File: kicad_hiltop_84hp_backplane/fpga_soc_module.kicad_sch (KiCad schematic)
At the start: 31 parts, among them J11 SO-DIMM

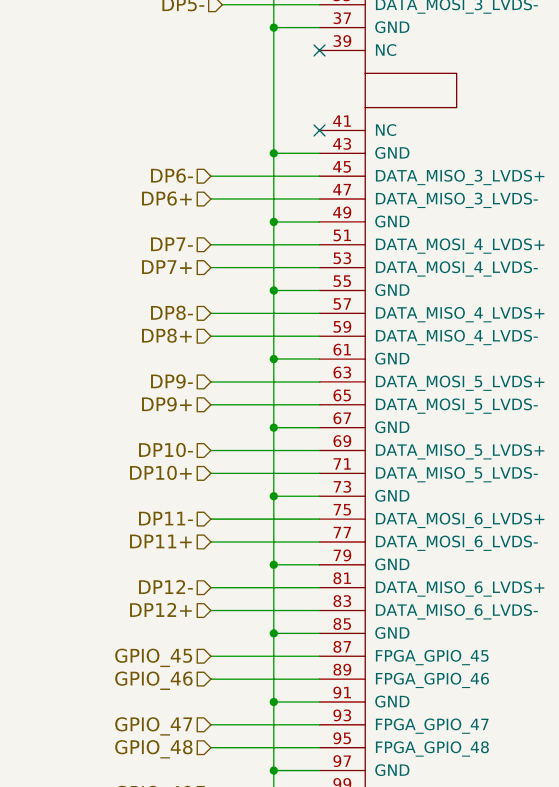
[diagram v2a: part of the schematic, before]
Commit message: Started differential tracking on layout
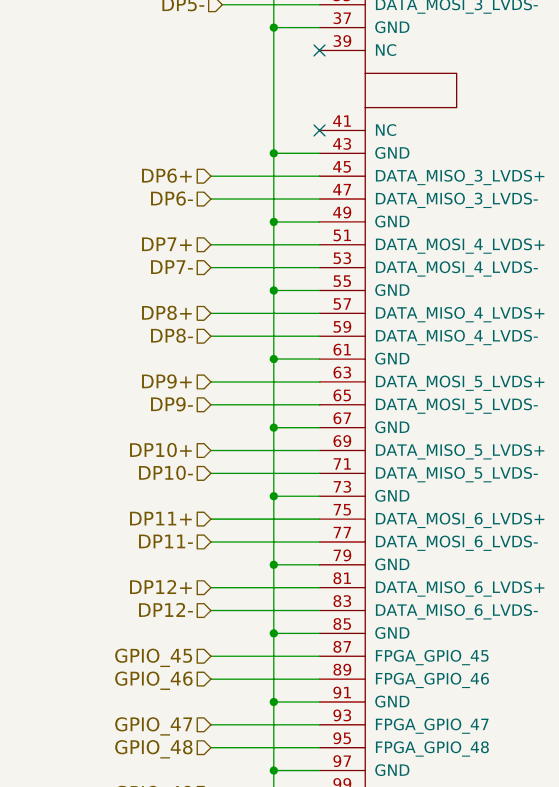
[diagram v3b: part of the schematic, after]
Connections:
- net DP10+: now also J11.69 (DATA_MISO_5_LVDS+); no longer J11.71 (DATA_MISO_5_LVDS-)
- net DP10-: now also J11.71 (DATA_MISO_5_LVDS-); no longer J11.69 (DATA_MISO_5_LVDS+)
- net DP11+: now also J11.75 (DATA_MOSI_6_LVDS+); no longer J11.77 (DATA_MOSI_6_LVDS-)
- net DP11-: now also J11.77 (DATA_MOSI_6_LVDS-); no longer J11.75 (DATA_MOSI_6_LVDS+)
- net DP12+: now also J11.81 (DATA_MISO_6_LVDS+); no longer J11.83 (DATA_MISO_6_LVDS-)
- net DP12-: now also J11.83 (DATA_MISO_6_LVDS-); no longer J11.81 (DATA_MISO_6_LVDS+)
- net DP6+: now also J11.45 (DATA_MISO_3_LVDS+); no longer J11.47 (DATA_MISO_3_LVDS-)
- net DP6-: now also J11.47 (DATA_MISO_3_LVDS-); no longer J11.45 (DATA_MISO_3_LVDS+)
- net DP7+: now also J11.51 (DATA_MOSI_4_LVDS+); no longer J11.53 (DATA_MOSI_4_LVDS-)
- net DP7-: now also J11.53 (DATA_MOSI_4_LVDS-); no longer J11.51 (DATA_MOSI_4_LVDS+)
- net DP8+: now also J11.57 (DATA_MISO_4_LVDS+); no longer J11.59 (DATA_MISO_4_LVDS-)
- net DP8-: now also J11.59 (DATA_MISO_4_LVDS-); no longer J11.57 (DATA_MISO_4_LVDS+)
- net DP9+: now also J11.63 (DATA_MOSI_5_LVDS+); no longer J11.65 (DATA_MOSI_5_LVDS-)
- net DP9-: now also J11.65 (DATA_MOSI_5_LVDS-); no longer J11.63 (DATA_MOSI_5_LVDS+)
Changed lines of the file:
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@@
     (effects (font (size 1.524 1.524)) (justify left))
   )
-  (hierarchical_label "DP6-" (shape input) (at 69.85 104.14 180)
+  (hierarchical_label "DP6-" (shape input) (at 69.85 106.68 180)
     (effects (font (size 1.524 1.524)) (justify right))
   )
@@
     (effects (font (size 1.524 1.524)) (justify left))
   )
-  (hierarchical_label "DP12-" (shape input) (at 69.85 149.86 180)
+  (hierarchical_label "DP12-" (shape input) (at 69.85 152.4 180)
     (effects (font (size 1.524 1.524)) (justify right))
   )
@@
     (effects (font (size 1.524 1.524)) (justify left))
   )
-  (hierarchical_label "DP10-" (shape input) (at 69.85 134.62 180)
+  (hierarchical_label "DP10-" (shape input) (at 69.85 137.16 180)
     (effects (font (size 1.524 1.524)) (justify right))
   )
@@
     (effects (font (size 1.524 1.524)) (justify left))
   )
-  (hierarchical_label "DP8-" (shape input) (at 69.85 119.38 180)
+  (hierarchical_label "DP8-" (shape input) (at 69.85 121.92 180)
     (effects (font (size 1.524 1.524)) (justify right))
   )
@@
     (effects (font (size 1.524 1.524)) (justify left))
   )
-  (hierarchical_label "DP6+" (shape input) (at 69.85 106.68 180)
+  (hierarchical_label "DP6+" (shape input) (at 69.85 104.14 180)
     (effects (font (size 1.524 1.524)) (justify right))
   )
@@
     (effects (font (size 1.524 1.524)) (justify right))
   )
-  (hierarchical_label "DP11+" (shape input) (at 69.85 144.78 180)
+  (hierarchical_label "DP11+" (shape input) (at 69.85 142.24 180)
     (effects (font (size 1.524 1.524)) (justify right))
   )
@@
     (effects (font (size 1.524 1.524)) (justify left))
   )
-  (hierarchical_label "DP7+" (shape input) (at 69.85 114.3 180)
+  (hierarchical_label "DP7+" (shape input) (at 69.85 111.76 180)
     (effects (font (size 1.524 1.524)) (justify right))
   )
@@
     (effects (font (size 1.524 1.524)) (justify left))
   )
-  (hierarchical_label "DP10+" (shape input) (at 69.85 137.16 180)
+  (hierarchical_label "DP10+" (shape input) (at 69.85 134.62 180)
     (effects (font (size 1.524 1.524)) (justify right))
   )
@@
     (effects (font (size 1.524 1.524)) (justify left))
   )
-  (hierarchical_label "DP9-" (shape input) (at 69.85 127 180)
+  (hierarchical_label "DP9-" (shape input) (at 69.85 129.54 180)
     (effects (font (size 1.524 1.524)) (justify right))
   )
@@
     (effects (font (size 1.524 1.524)) (justify right))
   )
-  (hierarchical_label "DP8+" (shape input) (at 69.85 121.92 180)
+  (hierarchical_label "DP8+" (shape input) (at 69.85 119.38 180)
     (effects (font (size 1.524 1.524)) (justify right))
   )
@@
     (effects (font (size 1.524 1.524)) (justify left))
   )
-  (hierarchical_label "DP7-" (shape input) (at 69.85 111.76 180)
+  (hierarchical_label "DP7-" (shape input) (at 69.85 114.3 180)
     (effects (font (size 1.524 1.524)) (justify right))
   )
@@
     (effects (font (size 1.524 1.524)) (justify left))
   )
-  (hierarchical_label "DP12+" (shape input) (at 69.85 152.4 180)
+  (hierarchical_label "DP12+" (shape input) (at 69.85 149.86 180)
     (effects (font (size 1.524 1.524)) (justify right))
   )
@@
     (effects (font (size 1.524 1.524)) (justify left))
   )
-  (hierarchical_label "DP11-" (shape input) (at 69.85 142.24 180)
+  (hierarchical_label "DP11-" (shape input) (at 69.85 144.78 180)
     (effects (font (size 1.524 1.524)) (justify right))
   )
@@
     (effects (font (size 1.524 1.524)) (justify right))
   )
-  (hierarchical_label "DP9+" (shape input) (at 69.85 129.54 180)
-    (effects (font (size 1.524 1.524)) (justify right))
-  )
+  (hierarchical_label "DP9+" (shape input) (at 69.85 127 180)
+    (effects (font (size 1.524 1.524)) (justify right))
+  )
